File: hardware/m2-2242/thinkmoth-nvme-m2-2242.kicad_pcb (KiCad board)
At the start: 2 copper layers, 31 x 68.4 mm, 18 parts, among them J2 ExpressCard, J3 MDT180M03001, U1 GL823K-HCY04

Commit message: updates
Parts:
- added R3: 0r, Resistor_SMD:R_0402_1005Metric, F.Cu at (62.9, 65.0)
- added R4: 0r, Resistor_SMD:R_0402_1005Metric, F.Cu at (62.3, 64.3)
- R1, R2: value 680r -> 4k
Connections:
- R1 pad 2: PCIe_LED -> PCIe_LED_S
- R2 pad 2: SD_LED -> SD_LED_S
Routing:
- net SD_LED_S: track 0.00 -> 81.6 mm, vias 0 -> 2
- net SD_LED: track 90.2 -> 11.2 mm, vias 2 -> 1
- net PCIe_LED_S: track 0.00 -> 51.8 mm, vias 0 -> 2
- net PCIe_LED: track 56.1 -> 7.95 mm, vias 2 -> 0
- net GND: track 0.00 -> 1.59 mm, vias 30 -> 31
- net SD_3V3: track 18.9 -> 18.1 mm
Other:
- board size 31 x 68.4 mm -> 31 x 63.4 mm
- board text added: "LED Jumpers R3: PCIe R4: uSD"
- board text added: "NVMe only!!!"

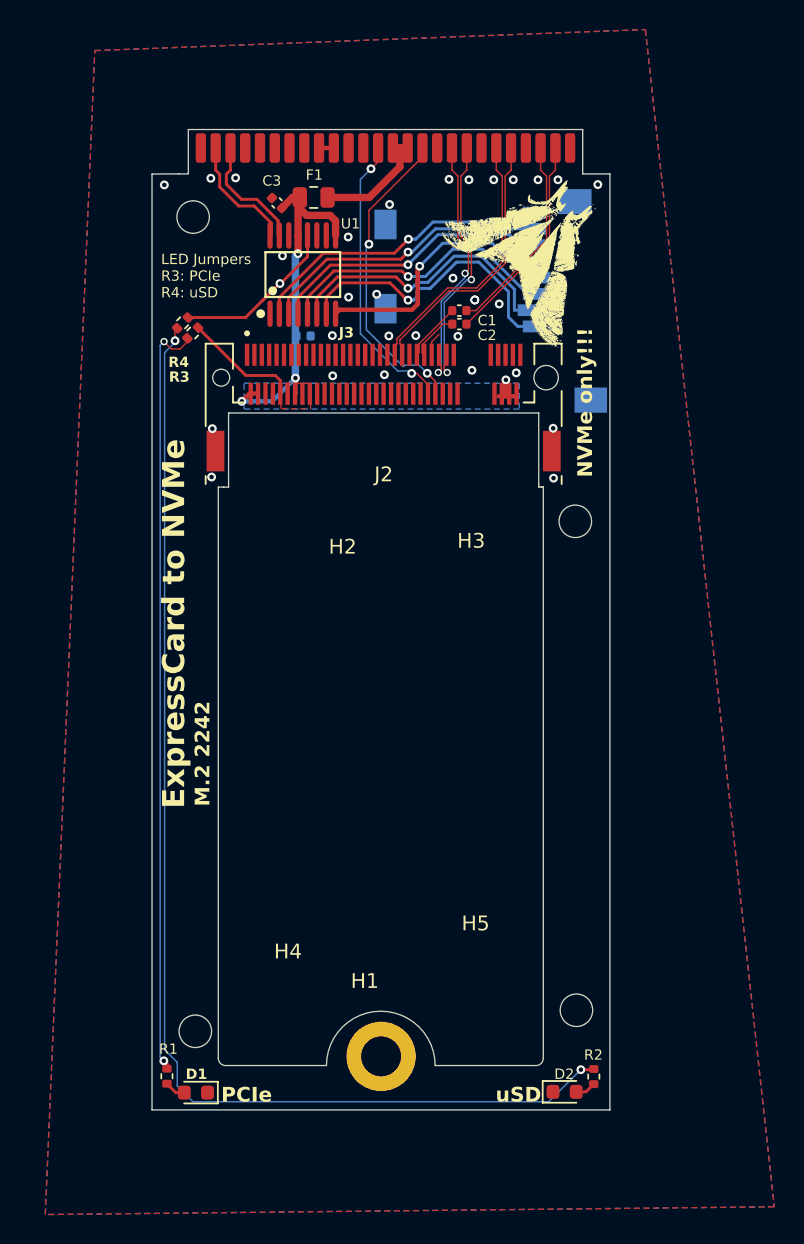
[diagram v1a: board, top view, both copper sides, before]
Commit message: combined m.2 2230 and 2242 design, wip
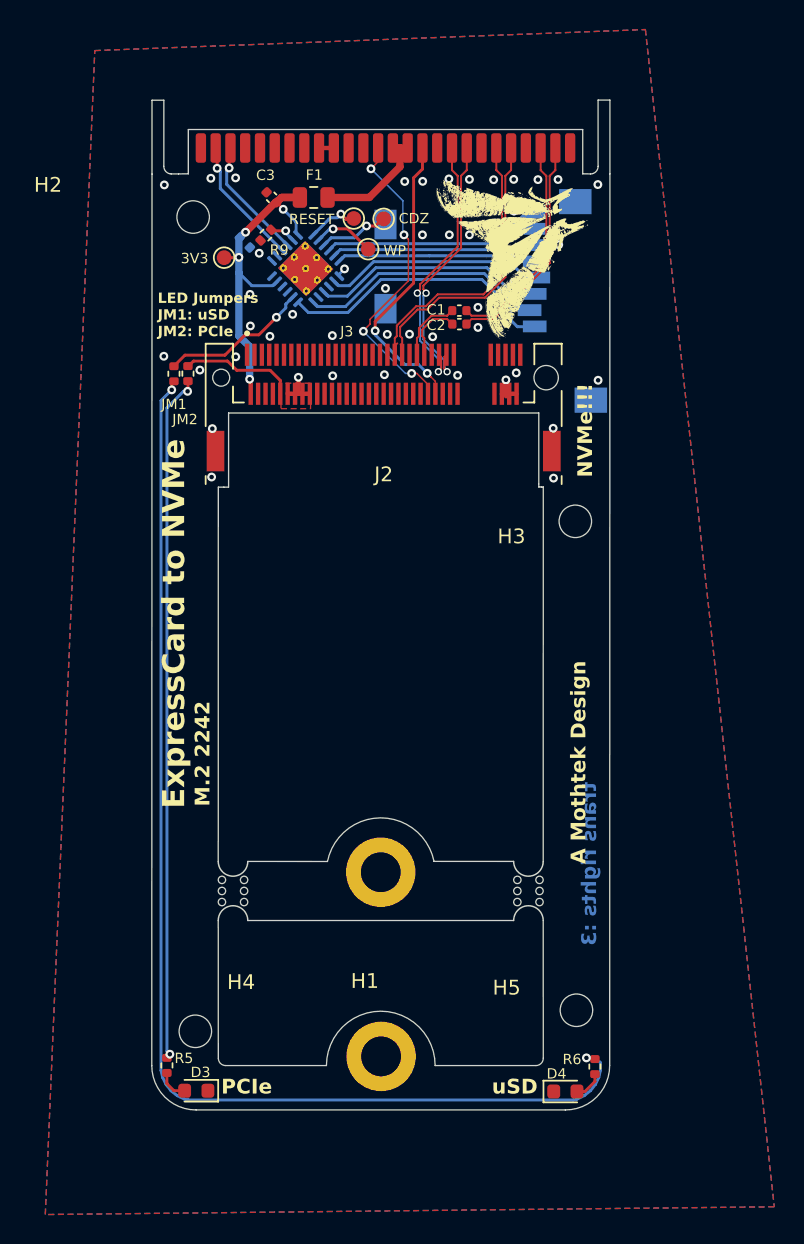
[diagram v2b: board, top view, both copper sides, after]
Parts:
- removed D1, D2: LED, LED_SMD:LED_0603_1608Metric
- removed R1, R2: 4k, Resistor_SMD:R_0402_1005Metric
- removed R3, R4: 0r, Resistor_SMD:R_0402_1005Metric
- removed U1: GL823K-HCY04, GL823K-HCY04:SSOP-16_L4.9-W3.9-P0.64-LS6.0-BL
- added 3V3: 3V3, TestPoint:TestPoint_Pad_D1.0mm, F.Cu at (65.1, 59.9)
- added ?: , , F.Cu at (75.7, 101.5)
- added CDZ: SD_CDZ, TestPoint:TestPoint_Pad_D1.0mm, F.Cu at (75.9, 57.3)
- added D3: LED, LED_SMD:LED_0603_1608Metric, F.Cu at (63.2, 116.3)
- added D4: LED, LED_SMD:LED_0603_1608Metric, F.Cu at (88.2, 116.4)
- added JM1: 0r, Resistor_SMD:R_0402_1005Metric, F.Cu at (61.7, 67.8)
- added JM2: 0r, Resistor_SMD:R_0402_1005Metric, F.Cu at (62.6, 67.8)
- added R5: 4kR, Resistor_SMD:R_0402_1005Metric, F.Cu at (61.2, 114.6)
- added R6: 4kR, Resistor_SMD:R_0402_1005Metric, F.Cu at (90.2, 114.7)
- added R9: 680r, Resistor_SMD:R_0402_1005Metric, F.Cu at (67.9, 58.4)
- added RESET: SD_RESET, TestPoint:TestPoint_Pad_D1.0mm, F.Cu at (73.8, 57.3)
- added U2: ~, Package_DFN_QFN:QFN-24-1EP_4x4mm_P0.5mm_EP2.7x2.6mm_ThermalVias, B.Cu at (70.6, 60.7)
- added WP: SD_WP, TestPoint:TestPoint_Pad_D1.0mm, F.Cu at (74.8, 59.4)
- added mouse-bite-2mm-slot: VAL**, Panelization.pretty-master:mouse-bite-2mm-slot, F.Cu at (65.7, 102.8)
- added mouse-bite-2mm-slot: VAL**, Panelization.pretty-master:mouse-bite-2mm-slot, F.Cu at (85.7, 102.8)
- moved C4 7.47 mm to (66.5, 58.9), turned to 135 degrees
- moved C3 0.53 mm to (68.3, 55.8)
- renumbered Card1 to SD1
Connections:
- J3 pad SH1: (no net) -> GND
- J3 pad SH2: (no net) -> GND
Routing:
- net SD_LED_S: track 81.6 -> 0.00 mm, vias 2 -> 0
- net Net-(JM1-Pad1): track 0.00 -> 81.1 mm, vias 0 -> 2
- net PCIe_LED_S: track 51.8 -> 0.00 mm, vias 2 -> 0
- net Net-(JM2-Pad1): track 0.00 -> 46.7 mm, vias 0 -> 2
- net 3V3: track 28.1 -> 37.1 mm, vias 4 -> 7
- net SD_CLK: track 20.2 -> 13.5 mm, vias 1 -> 0
- net SD_DAT1: track 20.8 -> 14.8 mm, vias 1 -> 0
- net SD_DAT0: track 19.7 -> 14.3 mm, vias 1 -> 0
- net SD_CDZ: track 0.00 -> 4.95 mm, vias 0 -> 1
- net SD_WP: track 0.00 -> 4.25 mm, vias 0 -> 1
- net SD_RESET: track 0.00 -> 3.49 mm, vias 0 -> 1
- net SD_CMD: track 19.4 -> 15.9 mm, vias 1 -> 0
- net SD_3V3: track 18.1 -> 15.1 mm, vias 1 -> 0
- net SD_DAT3: track 19.6 -> 16.7 mm, vias 1 -> 0
- net Net-(D3-A): track 0.00 -> 2.13 mm
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- added copper zone on In2.Cu, net 3V3
- added copper zone on In1.Cu, net GND
- removed copper zone on B.Cu, net 3V3
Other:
- board size 31 x 63.4 mm -> 31 x 68.4 mm
- copper layers 2 -> 4
- board text added: "A Mothtek Design"
- board text added: "LED Jumpers JM1: uSD JM2: PCIe"
- board text added: "Moth"
- board text added: "NVMe!!!"
- board text added: "Think"
- board text removed: "By Mothtek"
- board text removed: "LED Jumpers R3: PCIe R4: uSD"
- board text removed: "NVMe only!!!"
- board text removed: "ThinkMoth"
